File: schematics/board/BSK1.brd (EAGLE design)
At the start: 82 x 100 mm, 34 parts

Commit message: Сделаны платы CROSSnew, SPIDERnew, BSK2
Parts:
- removed DS18B20Z1: DS18B20Z, CanCubeSat:SOIC8+HEAT_S
- removed U$15: GRAFITGRAFIT3_1, CanCubeSat:GRAFIT3_1
- removed YELLOW: LAP4-BOTTOM, led:P47F-BOTTOM
- added DS18B20Z: DS18B20Z, CanCubeSat:DS18B20Z
- added JP1, JP2, JP3, JP4, JP5, JP6: (no value), pinheadCS:2X10
- added LAP1: LAP4-BOTTOM, led:P47F-BOTTOM
- added U$17: GRAFITGRAFIT3_1, CanCubeSat:GRAFIT3_1
- BKU: device pinheadCS:1X08 -> pinheadCS:1X20
- moved R14 156.5 mm to (-13.1, -88.1)
- moved R13 155.1 mm to (-8.10, -82.8)
- moved U$13 152.9 mm to (-10.9, -82.5)
- moved LED7 151.9 mm to (-5.60, -78.1), turned to 0 degrees
- moved LED6 137.4 mm to (-12.1, -67.6)
- moved R7 136.3 mm to (-9.50, -66.4), turned to 0 degrees
- moved U$26 130.2 mm to (-0.97, -40.5), turned to 0 degrees
- moved R8 130.0 mm to (-13.1, -71.9)
- moved U$14 127.6 mm to (-11.2, -61.8)
- moved U$8 114.7 mm to (-6.00, -54.7)
- moved R12 113.1 mm to (1.50, -19.9), turned to 0 degrees
- moved R5 107.2 mm to (1.50, -15.0), turned to 0 degrees
- moved R94 106.6 mm to (7.20, -19.9), turned to 0 degrees
- moved R6 106.6 mm to (7.20, -15.0), turned to 0 degrees
- moved R9 106.4 mm to (12.9, -15.0), turned to 0 degrees
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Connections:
- net B2-CMD renamed B1-CMD
- net B2-KHEAT renamed B1-KHEAT
- net B2-KVCC renamed B1-KVCC
- net B2-ROZE renamed B1-ROZE
- new net 3V3: BKU.8, JP1.9, JP2.9, JP3.9, JP4.9, JP5.9, JP6.9
- new net BMS1: JP1.1, JP2.1, JP3.1, JP4.5, JP5.3, JP6.3
- new net BMS2: JP1.2, JP2.2, JP3.2, JP4.6, JP5.4, JP6.4
- new net BMS3: JP1.3, JP2.3, JP3.3, JP4.1, JP5.5, JP6.5
- new net BMS4: JP1.4, JP2.4, JP3.4, JP4.2, JP5.6, JP6.6
- new net BMS5: JP1.5, JP2.5, JP3.5, JP4.3, JP5.1, JP6.1
- new net BMS6: JP1.6, JP2.6, JP3.6, JP4.4, JP5.2, JP6.2
- new net I2CINT: BKU.13
- new net INT: JP1.16, JP2.16, JP3.16, JP4.16, JP5.16, JP6.16
- new net N$1: DS18B20Z.HEAT, U$26.HEAT
- new net PL1: JP1.17, JP2.17, JP3.17, JP4.17, JP5.17, JP6.17
- new net PL1-KVCC: BKU.15
- new net PL2: JP1.19, JP2.19, JP3.19, JP4.19, JP5.19, JP6.19
- new net PL2-KVCC: BKU.16
- new net PL3: JP1.18, JP2.18, JP3.18, JP4.18, JP5.18, JP6.18
- new net PL3-KVCC: BKU.17
- new net PL4: JP1.20, JP2.20, JP3.20, JP4.20, JP5.20, JP6.20
- new net PL4-KVCC: BKU.18
- new net PL5-KVCC: BKU.19
- new net PL6-KVCC: BKU.20
- new net SCL: BKU.10, JP1.13, JP2.13, JP3.13, JP4.13, JP5.13, JP6.13
- new net SDA: BKU.12, JP1.14, JP2.14, JP3.14, JP4.14, JP5.14, JP6.14
- new net TIME: BKU.14, JP1.15, JP2.15, JP3.15, JP4.15, JP5.15, JP6.15
- net 1W: now also DS18B20Z.4, JP1.7, JP2.7, JP3.7, JP4.7, JP5.7, JP6.7; no longer DS18B20Z1.4
- net 2: now also U$17.P$1; no longer U$15.P$1
- net 5V: now also DS18B20Z.3, JP1.10, JP2.10, JP3.10, JP4.10, JP5.10, JP6.10; no longer DS18B20Z1.3
- net BUS+: now also JP1.8, JP2.8, JP3.8, JP4.8, JP5.8, JP6.8, U$17.P$2; no longer U$15.P$2
- net BUS-: now also LAP1.C; no longer YELLOW.C
- net GND: now also BKU.11, BKU.9, DS18B20Z.5, JP1.11, JP1.12, JP2.11, JP2.12, JP3.11, JP3.12, JP4.11, JP4.12, JP5.11, JP5.12, JP6.11, JP6.12; no longer BKU.8, DS18B20Z1.5, DS18B20Z1.HEAT, U$26.HEAT
- net N$28: now also LAP1.A; no longer YELLOW.A
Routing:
- net BUS+: track 226.1 -> 0.00 mm, vias 2 -> 0
- net 2: track 160.0 -> 0.00 mm, vias 2 -> 0
- net BUS-: track 117.3 -> 0.00 mm, vias 2 -> 0
- net 5V: track 112.3 -> 0.00 mm, vias 6 -> 0
- net B1-CMD: track 74.1 -> 0.00 mm, vias 2 -> 0
- net B1-ROZE: track 72.6 -> 0.00 mm, vias 2 -> 0
- net B1-KHEAT: track 50.0 -> 0.00 mm, vias 1 -> 0
- net B1-KVCC: track 35.1 -> 0.00 mm
- net 1W: track 30.4 -> 0.00 mm, vias 2 -> 0
- net BUS-1: track 23.4 -> 0.00 mm
- net BUS-2: track 23.4 -> 0.00 mm
- net BUS-3: track 23.3 -> 0.00 mm
- net BUS+1: track 22.1 -> 0.00 mm
- net BUS+2: track 22.1 -> 0.00 mm
- net BUS+3: track 22.0 -> 0.00 mm
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- removed copper zone on layer 1, net GND1
- removed copper zone on layer 1, net GND2
- removed copper zone on layer 1, net GND3
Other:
- outline, holes or cut-outs redrawn
- board text added: "BUS"

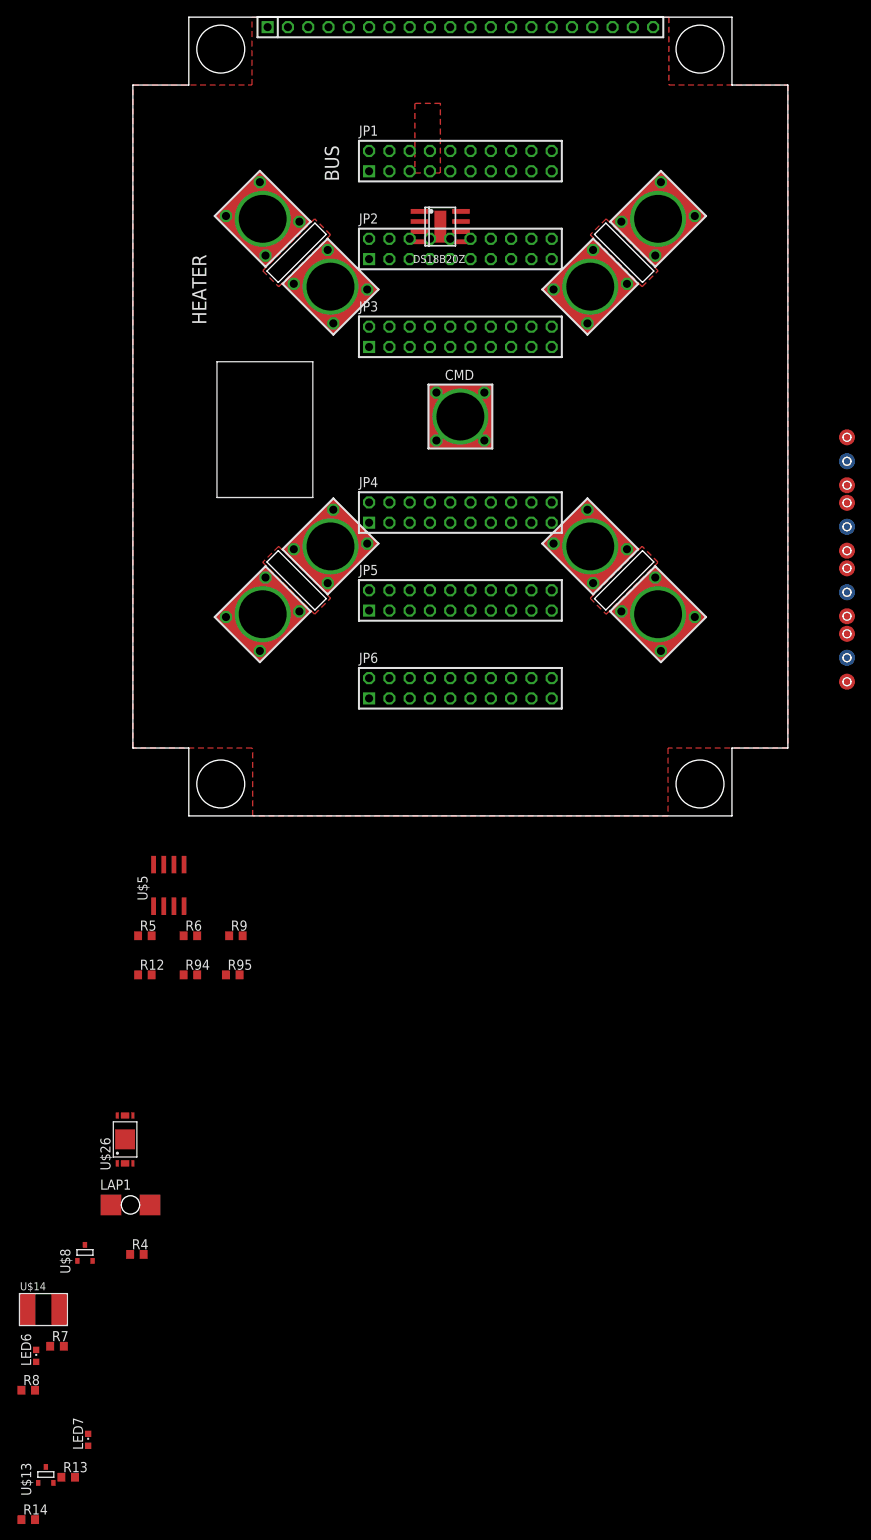
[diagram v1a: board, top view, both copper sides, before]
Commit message: Добавлены предохранители в библиотеку
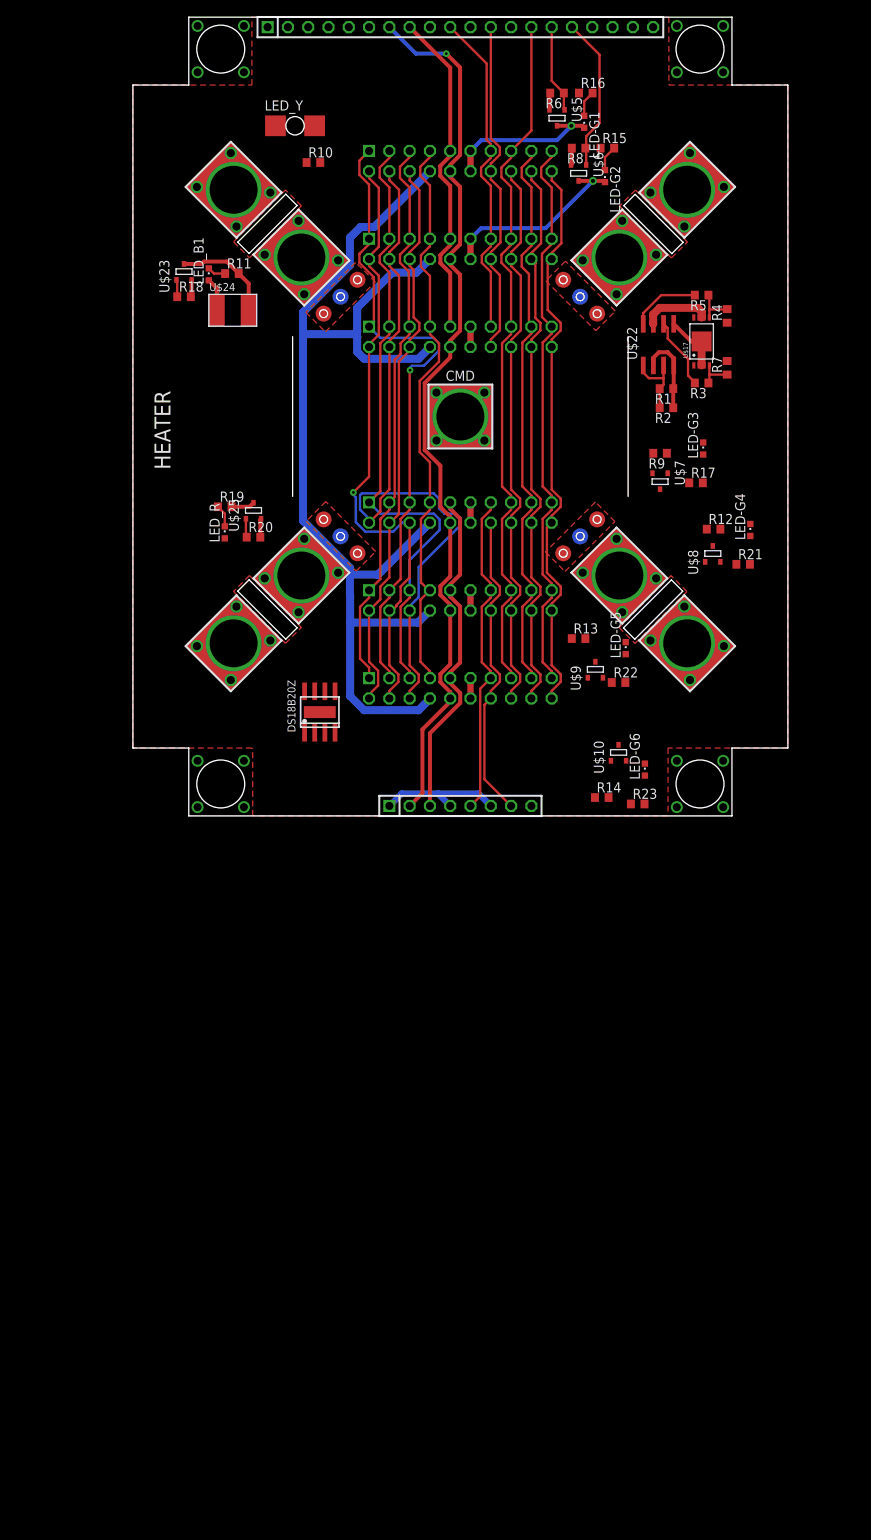
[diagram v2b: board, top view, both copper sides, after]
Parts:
- removed LAP1: LAP4-BOTTOM, led:P47F-BOTTOM
- removed LED6, LED7: (no value), led:CHIPLED_0603
- removed R94, R95: 2k26, resistor:R0603
- removed U$11, U$12: KCONNECT, CanCubeSat:KCONNECT
- removed U$13: SI2302CDS, CanCubeSat:SOT23-3
- removed U$14: EM_HEAT, CanCubeSat:EM_HEAT
- removed U$16: GRAFITGRAFIT3_1, CanCubeSat:GRAFIT3_1
- removed U$26: FS8205A+, CanCubeSat:FS8205A+
- added BSK5: (no value), pinheadCS:1X08
- added LED-G1, LED-G2, LED-G3, LED-G4, LED-G5, LED-G6, LED_B1, LED_R: (no value), led:CHIPLED_0603
- added LED_Y: LAP4-BOTTOM, led:P47F-BOTTOM
- added R1, R2: 2k26, resistor:R0603
- added R10, R11, R15, R16, R17, R21, R22, R23: 2k, resistor:R0603
- added R18, R20, R3: 1M, resistor:R0603
- added R19: 1k5, resistor:R0603
- added U$18, U$19, U$20, U$21: KCONNECT, CanCubeSat:KCONNECT
- added U$22: MOCD217M, CanCubeSat:SOIC8
- added U$23, U$25: SI2302CDS, CanCubeSat:SOT23-3
- added U$24: EM_HEAT, CanCubeSat:EM_HEAT
- added U$27, U$28, U$29, U$30: GRAFITGRAFIT3_1, CanCubeSat:GRAFIT3_1
- R12, R6: value 2M -> 1M
- R13: value 1k5 -> 1M
- R4, R7: value 2k -> 2M
- U$10, U$9: value KCONNECT -> SI2302CDS; device CanCubeSat:KCONNECT -> CanCubeSat:SOT23-3
- U$17: value GRAFITGRAFIT3_1 -> FS8205A+; device CanCubeSat:GRAFIT3_1 -> CanCubeSat:FS8205A+
- U$5: value MOCD217M -> SI2302CDS; device CanCubeSat:SOIC8 -> CanCubeSat:SOT23-3
- U$6, U$7: value GRAFITGRAFIT3_1 -> SI2302CDS; device CanCubeSat:GRAFIT3_1 -> CanCubeSat:SOT23-3
- moved R8 170.1 mm to (55.8, 83.6), turned to 180 degrees
- moved R7 148.5 mm to (74.4, 56.1), turned to 90 degrees
- moved R4 138.8 mm to (74.4, 62.6), turned to 90 degrees
- moved R13 122.9 mm to (55.8, 22.2)
- moved U$8 117.6 mm to (72.6, 32.8)
- moved R14 115.4 mm to (58.7, 2.30)
- moved R6 115.1 mm to (53.1, 90.5), turned to 180 degrees
- moved U$5 107.7 mm to (53.1, 87.4), turned to 180 degrees
- moved R5 106.3 mm to (71.2, 65.2), turned to 180 degrees
- moved R12 90.5 mm to (72.7, 35.9)
- moved R9 80.4 mm to (66.0, 45.4), turned to 180 degrees
- moved DS18B20Z 62.6 mm to (23.4, 13.0), turned to 0 degrees
- moved U$6 49.3 mm to (55.8, 80.5), turned to 180 degrees
- moved U$10 44.4 mm to (60.8, 7.90), turned to 0 degrees
- moved U$17 43.6 mm to (71.2, 59.4)
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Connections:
- removed net 1: R7.2, U$14.2, U$8.3
- removed net 2: R13.2, U$13.3, U$16.P$1, U$17.P$1, U$6.P$1, U$7.P$1
- removed net I2CINT: BKU.13
- removed net N$26: R5.1, R6.2, U$26.5
- removed net N$29: LED7.C, R13.1
- removed net N$31: LED6.C, R7.1
- removed net OC1: R9.2, U$5.6
- removed net OD1: R5.2, U$5.8
- new net 3: R11.2, U$23.3, U$24.2
- new net 4: R19.2, U$25.3, U$27.P$1, U$28.P$1, U$29.P$1, U$30.P$1
- new net N$2: LED_B1.C, R11.1
- new net N$21: LED-G3.A, R17.2
- new net N$22: LED-G4.A, R21.2
- new net N$23: LED-G5.A, R22.2
- new net N$24: LED-G6.A, R23.2
- new net N$3: LED_R.C, R19.1
- new net N$38: LED-G2.A, R15.2
- new net N$4: LED-G1.A, R16.2
- new net OC2: R3.2, U$22.6
- new net OD2: R5.2, U$22.8
- new net PL1-GND: JP1.11, JP1.12, LED-G1.C, U$5.3
- new net PL2-GND: JP2.11, JP2.12, LED-G2.C, U$6.3
- new net PL3-GND: JP3.11, JP3.12, LED-G3.C, U$7.3
- new net PL4-GND: JP4.11, JP4.12, LED-G4.C, U$8.3
- new net PL5-GND: JP5.11, JP5.12, LED-G5.C, U$9.3
- new net PL6-GND: JP6.11, JP6.12, LED-G6.C, U$10.3
- new net TIME-ES: BKU.13, BSK5.8
- net 3V3: now also BSK5.3
- net 5V: now also BSK5.2, LED_B1.A, R10.1, R15.1, R16.1, R17.1, R21.1, R22.1, R23.1, U$24.1; no longer LED6.A, R4.1, U$14.1
- net B1-KHEAT: now also R18.1, U$23.1; no longer R8.1, U$8.1
- net B1-KVCC: now also R1.2, R2.2, U$22.1, U$22.3; no longer R94.2, R95.2, U$5.1, U$5.3
- net B1-ROZE: now also R20.1, U$25.1; no longer R14.1, U$13.1
- net BUS+: now also LED_R.A, R4.1, R7.2, U$27.P$2, U$28.P$2, U$29.P$2, U$30.P$2; no longer LED7.A, R12.2, R6.1, U$16.P$2, U$17.P$2, U$6.P$2, U$7.P$2
- net BUS+2: now also U$18.1, U$18.2, U$18.3, U$18.4, U$18.P$1, U$18.P$2; no longer U$9.1, U$9.2, U$9.3, U$9.4, U$9.P$1, U$9.P$2
- net BUS+3: now also U$20.1, U$20.2, U$20.3, U$20.4, U$20.P$1, U$20.P$2; no longer U$11.1, U$11.2, U$11.3, U$11.4, U$11.P$1, U$11.P$2
- net BUS-: now also LED_Y.C, U$17.67, U$22.7; no longer LAP1.C, U$26.67, U$5.7
- net BUS-2: now also U$19.1, U$19.2, U$19.3, U$19.4, U$19.P$1, U$19.P$2; no longer U$10.1, U$10.2, U$10.3, U$10.4, U$10.P$1, U$10.P$2
- net BUS-3: now also U$21.1, U$21.2, U$21.3, U$21.4, U$21.P$1, U$21.P$2; no longer U$12.1, U$12.2, U$12.3, U$12.4, U$12.P$1, U$12.P$2
- net GND: now also BSK5.1, BSK5.4, BSK5.6, DS18B20Z.HEAT, R1.1, R12.2, R13.2, R18.2, R2.1, R20.2, R6.2, R9.2, U$10.2, U$17.23, U$17.HEAT, U$22.2, U$22.4, U$22.5, U$23.2, U$25.2, U$6.2, U$7.2, U$9.2; no longer JP1.11, JP1.12, JP2.11, JP2.12, JP3.11, JP3.12, JP4.11, JP4.12, JP5.11, JP5.12, JP6.11, JP6.12, R94.1, R95.1, U$13.2, U$26.23, U$5.4, U$5.5
- net N$1: now also R4.2, R5.1, U$17.5; no longer DS18B20Z.HEAT, U$26.HEAT
- net N$27: now also R3.1, R7.1, U$17.4; no longer R12.1, R9.1, U$26.4
- net N$28: now also LED_Y.A, R10.2; no longer LAP1.A, R4.2
- net PL1-KVCC: now also R6.1, U$5.1
- net PL2-KVCC: now also R8.1, U$6.1
- net PL3-KVCC: now also R9.1, U$7.1
- net PL4-KVCC: now also R12.1, U$8.1
- net PL5-KVCC: now also R13.1, U$9.1
- net PL6-KVCC: now also R14.1, U$10.1
- net SCL: now also BSK5.5
- net SDA: now also BSK5.7
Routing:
- net BUS+: track 0.00 -> 144.4 mm
- net 5V: track 0.00 -> 116.9 mm, vias 0 -> 1
- net BMS4: track 0.00 -> 91.5 mm
- net TIME: track 0.00 -> 87.4 mm
- net 3V3: track 0.00 -> 83.8 mm
- net SCL: track 0.00 -> 82.5 mm
- net SDA: track 0.00 -> 82.0 mm
- net BMS1: track 0.00 -> 80.4 mm, vias 0 -> 1
- net BMS3: track 0.00 -> 79.1 mm
- net BMS2: track 0.00 -> 78.9 mm, vias 0 -> 1
- net 1W: track 0.00 -> 71.9 mm
- net PL4: track 0.00 -> 71.7 mm
- net PL3: track 0.00 -> 71.6 mm
- net BMS6: track 0.00 -> 71.2 mm
- net BMS5: track 0.00 -> 71.1 mm
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- added copper zone on layer 1, net GND1
- added copper zone on layer 1, net GND2
- added copper zone on layer 1, net GND3
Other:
- outline, holes or cut-outs redrawn
- board text added: "BSK1 "Концерн ИТС""
- board text added: "to BSK5"
- board text removed: "BSK2 "Концерн ИТС""
- board text removed: "BUS"

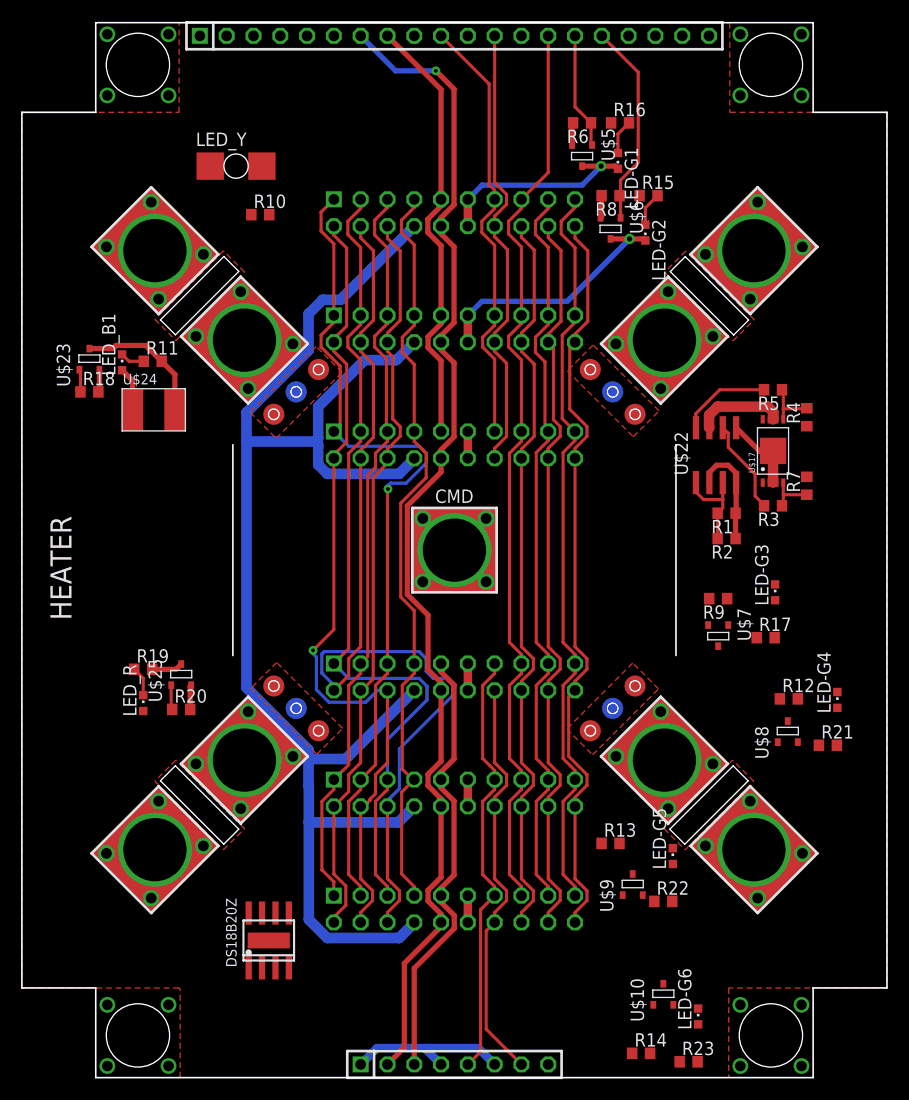
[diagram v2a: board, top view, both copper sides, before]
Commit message: Разведена БСК1
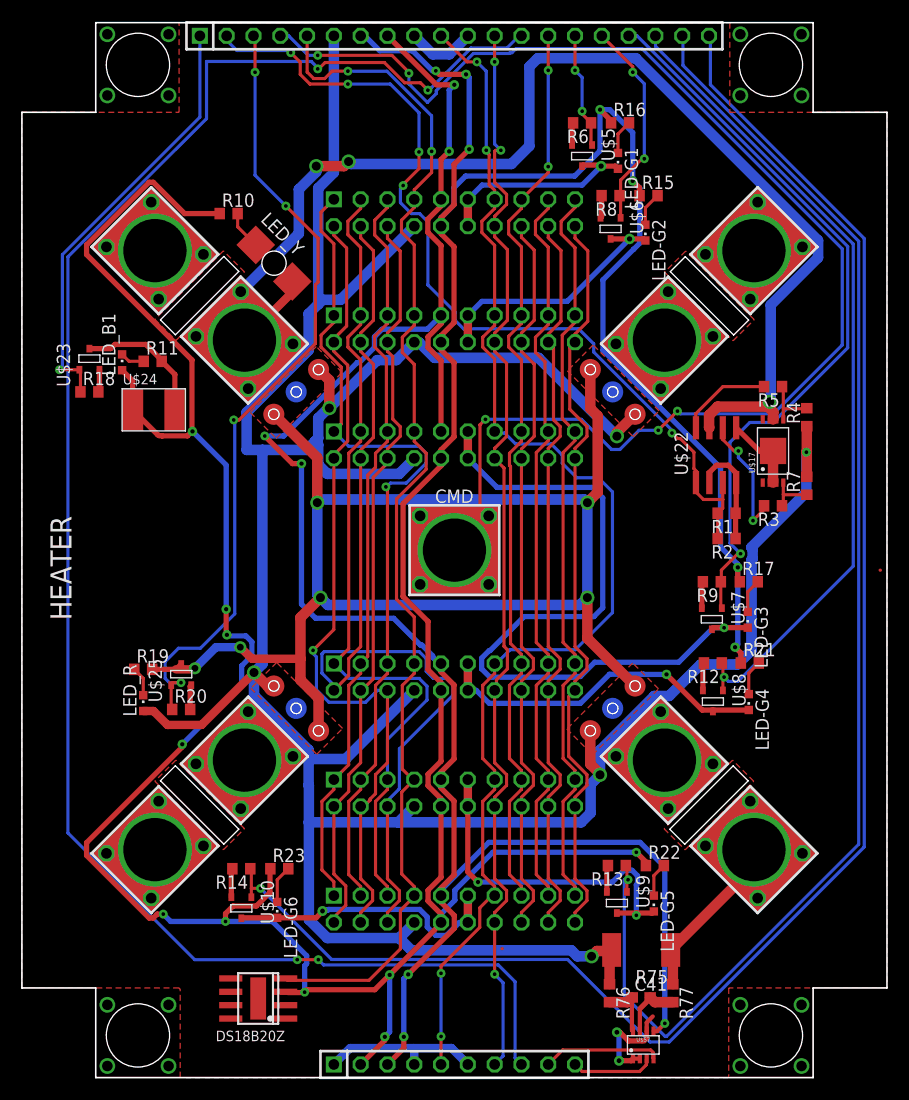
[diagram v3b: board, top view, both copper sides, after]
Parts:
- added C41: 0,1µ, rcl:C0603
- added R75: R01, rcl:R2512
- added R76, R77: 10R, resistor:R0603
- added U$57: INA219AID, CanCubeSat:SOT23-8
- BSK5: device pinheadCS:1X08 -> pinheadCS:1X10
- DS18B20Z: device CanCubeSat:DS18B20Z -> CanCubeSat:SOIC8+HEAT_S
- moved R23 42.9 mm to (24.4, 19.8)
- moved R14 41.7 mm to (20.8, 19.8), turned to 180 degrees
- moved LED-G6 41.2 mm to (24.2, 15.9), turned to 180 degrees
- moved U$10 40.8 mm to (20.8, 16.1), turned to 180 degrees
- moved R21 10.8 mm to (69.0, 39.3)
- moved LED_Y 9.88 mm to (23.9, 77.2), turned to 315 degrees
- moved LED-G4 8.40 mm to (68.9, 35.6), turned to 180 degrees
- moved R12 7.96 mm to (65.5, 39.3), turned to 180 degrees
- moved U$8 7.67 mm to (65.5, 35.7), turned to 180 degrees
- moved DS18B20Z 5.59 mm to (22.4, 7.50), turned to 90 degrees
- moved R17 5.54 mm to (68.9, 47.0)
- moved LED-G5 4.85 mm to (59.9, 16.5), turned to 180 degrees
- moved LED-G3 3.68 mm to (68.8, 43.4), turned to 180 degrees
- moved R22 3.49 mm to (60.0, 20.1)
- moved R10 3.00 mm to (19.6, 81.9)
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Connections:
- net BUS+1 renamed SP+1
- net BUS+2 renamed SP+3
- net BUS- renamed SP-
- net BUS-1 renamed SP-1
- net BUS-2 renamed SP-2
- net BUS-3 renamed SP-3
- net SCL renamed SCL-TM
- net SDA renamed SDA-TM
- removed net BUS+3: U$20.1, U$20.2, U$20.3, U$20.4, U$20.P$1, U$20.P$2
- new net N$150: C41.1, R76.2, U$57.8
- new net N$151: C41.2, R77.2, U$57.7
- new net SCL-INA: BSK5.9, U$57.4
- new net SDA-INA: BSK5.10, U$57.3
- new net SP+: R75.1, R77.1, U$20.1, U$20.2, U$20.3, U$20.4, U$20.P$1, U$20.P$2
- new net SP+2: U$3.1, U$3.2, U$3.3, U$3.4, U$3.P$1, U$3.P$2
- net 3V3: now also U$57.5
- net BUS+: now also R75.2, R76.1; no longer U$3.1, U$3.2, U$3.3, U$3.4, U$3.P$1, U$3.P$2
- net GND: now also U$57.1, U$57.2, U$57.6
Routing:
- net 5V: track 116.9 -> 377.0 mm, vias 1 -> 17
- net BUS+: track 144.4 -> 313.6 mm, vias 0 -> 6
- net TIME-ES: track 0.00 -> 168.6 mm, vias 0 -> 4
- net PL6-KVCC: track 0.00 -> 157.5 mm, vias 0 -> 1
- net B1-CMD: track 0.00 -> 143.7 mm, vias 0 -> 5
- net 4: track 2.96 -> 133.7 mm, vias 0 -> 6
- net PL5-KVCC: track 0.00 -> 128.9 mm, vias 0 -> 1
- net SP-: track 8.54 -> 134.3 mm, vias 0 -> 3
- net 3V3: track 83.8 -> 183.2 mm, vias 0 -> 7
- net PL4-KVCC: track 0.00 -> 77.7 mm, vias 0 -> 1
- net B1-KVCC: track 9.23 -> 85.9 mm, vias 0 -> 5
- net B1-ROZE: track 2.34 -> 76.1 mm, vias 0 -> 4
- net PL3-KVCC: track 0.00 -> 70.6 mm, vias 0 -> 1
- net PL3-GND: track 2.54 -> 70.5 mm, vias 0 -> 1
- net 1W: track 71.9 -> 116.1 mm, vias 0 -> 2
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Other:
- outline, holes or cut-outs redrawn
